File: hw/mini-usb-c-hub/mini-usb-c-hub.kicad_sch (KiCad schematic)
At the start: 26 parts, among them J1 USB_C_Receptacle_USB2.0_16P, U101 FE1.1s, Y101 12MHz

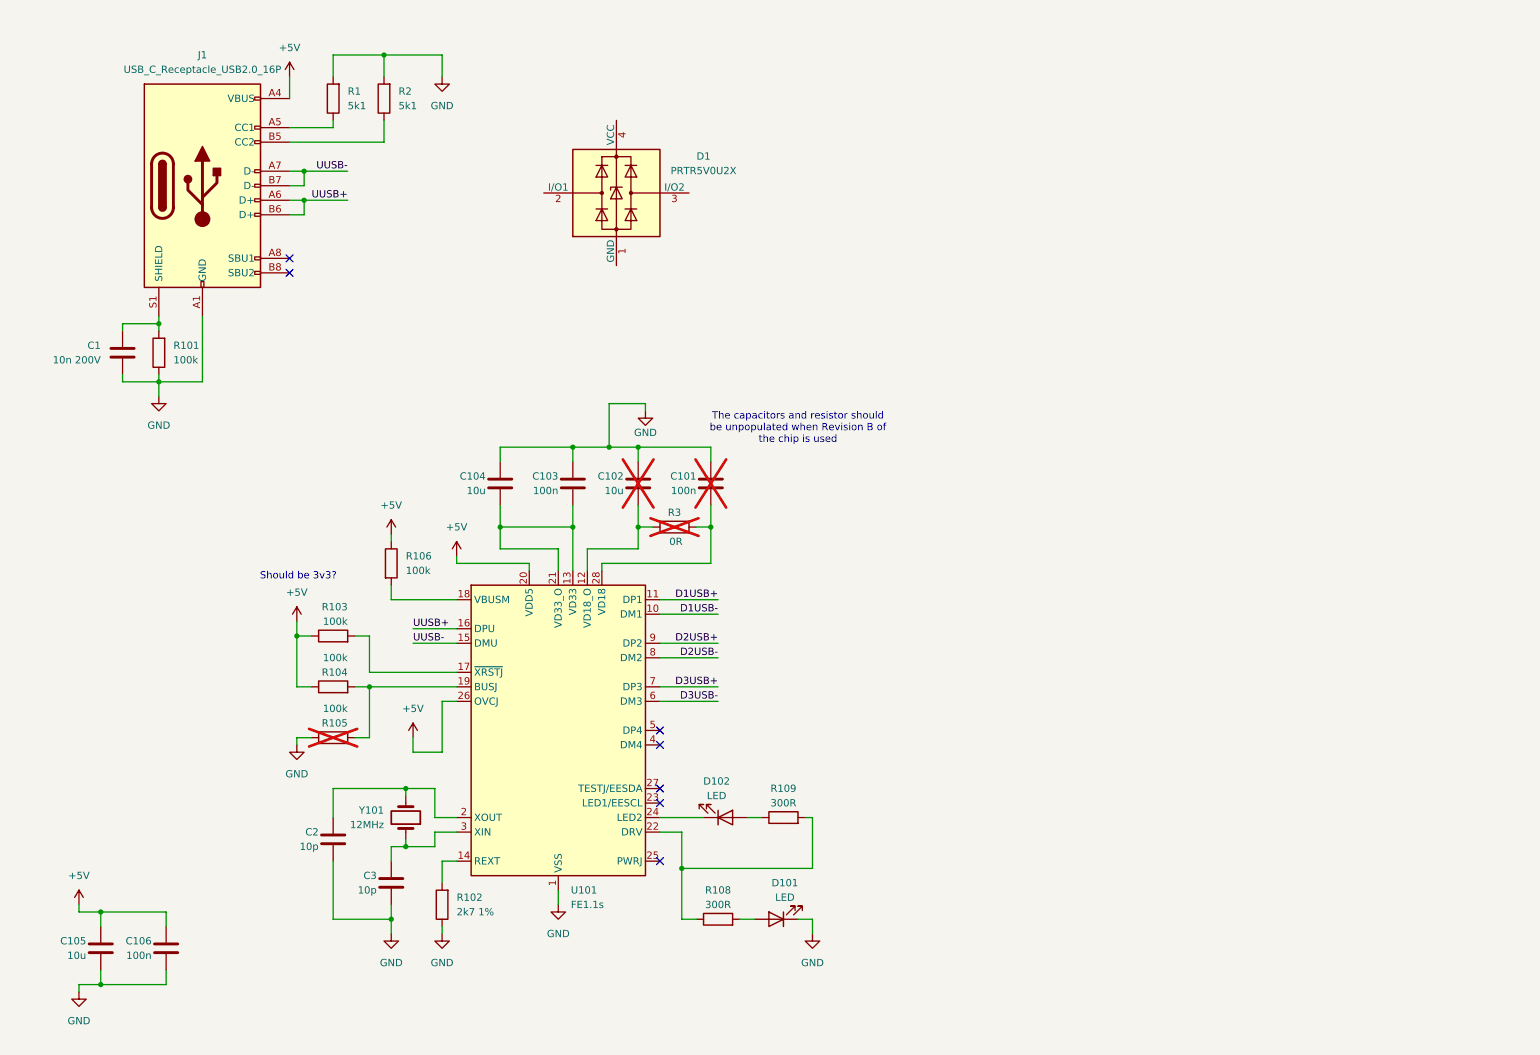
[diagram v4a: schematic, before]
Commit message: chore(hw): add downstream ports
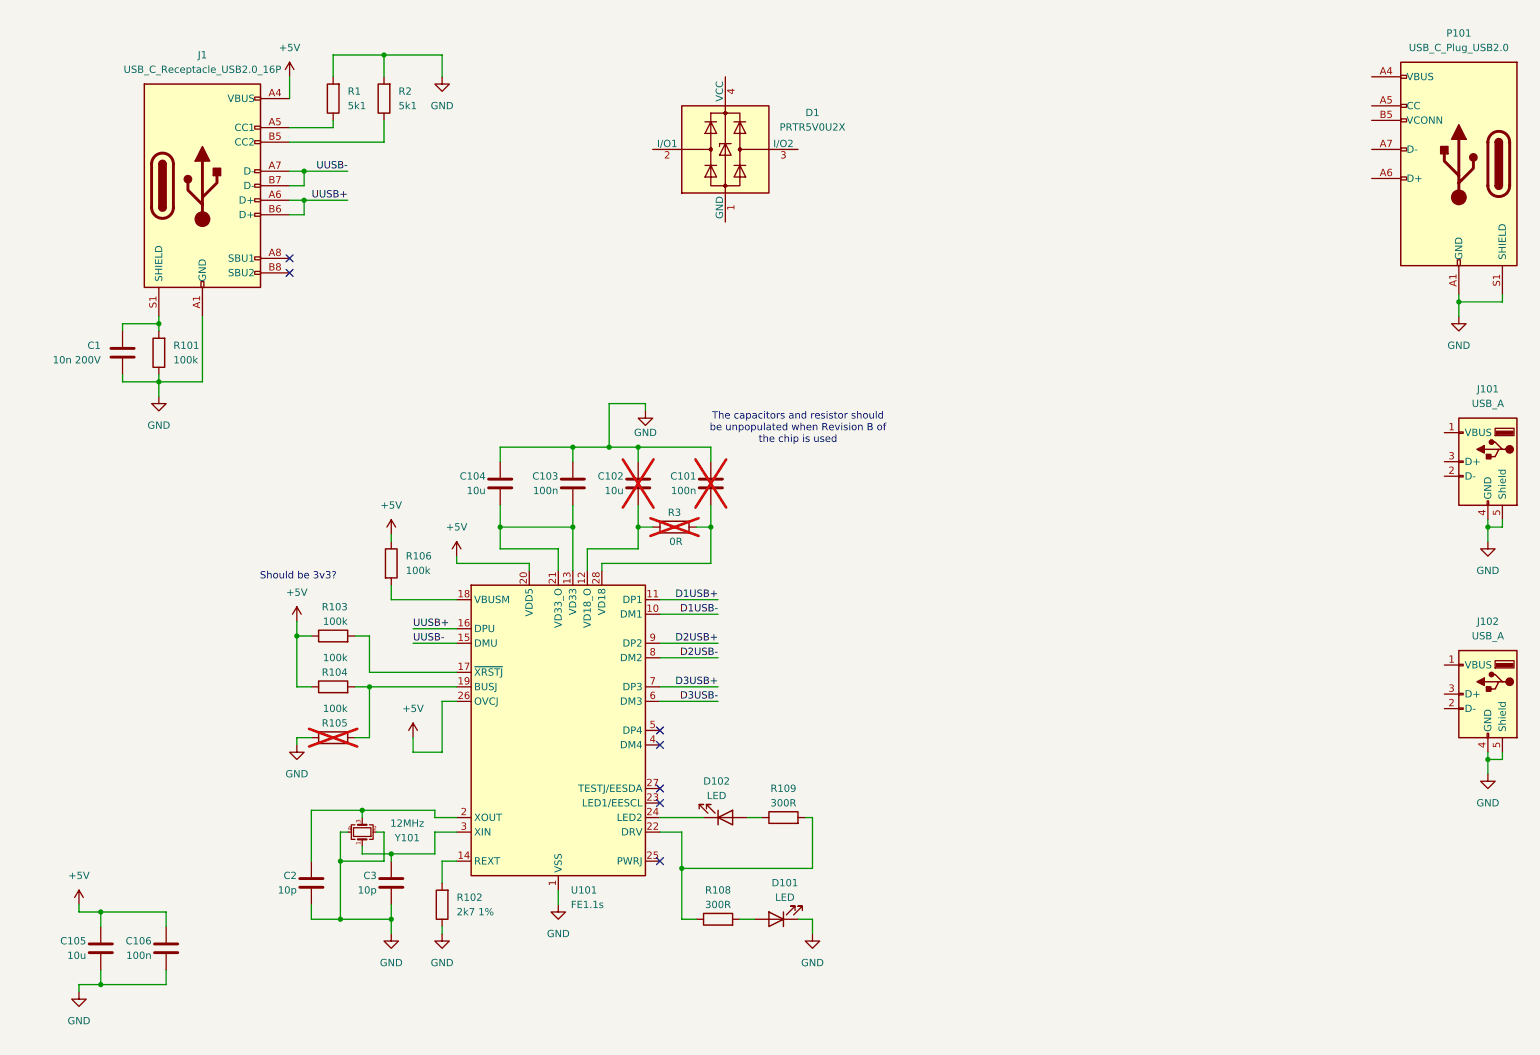
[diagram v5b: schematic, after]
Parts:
- removed Y101: 12MHz, symbol Device:Crystal
- added J101, J102: USB_A, Connector_USB:USB_A_Molex_67643_Horizontal, symbol Connector:USB_A
- added P101: USB_C_Plug_USB2.0, symbol Connector:USB_C_Plug_USB2.0
- added Y101: 12MHz, Crystal:Crystal_SMD_3225-4Pin_3.2x2.5mm_HandSoldering, symbol Device:Crystal_GND24_Small
- D101, D102: footprint (none) -> LED_SMD:LED_0805_2012Metric_Pad1.15x1.40mm_HandSolder
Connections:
- net GND: now also J101.4 (GND), J101.5 (Shield), J102.4 (GND), J102.5 (Shield), P101.A1 (GND), P101.A12 (GND), P101.B1 (GND), P101.B12 (GND), P101.S1 (SHIELD), Y101.2, Y101.4
- net at C2.2, U101.2 (XOUT): now also Y101.3
- net at C3.2, U101.3 (XIN): now also Y101.1
- new net: P101.A4 (VBUS), P101.A9 (VBUS), P101.B4 (VBUS), P101.B9 (VBUS)
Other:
- moved on the sheet: C2, D1

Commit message: chore(hw): add USB-C plug symbol
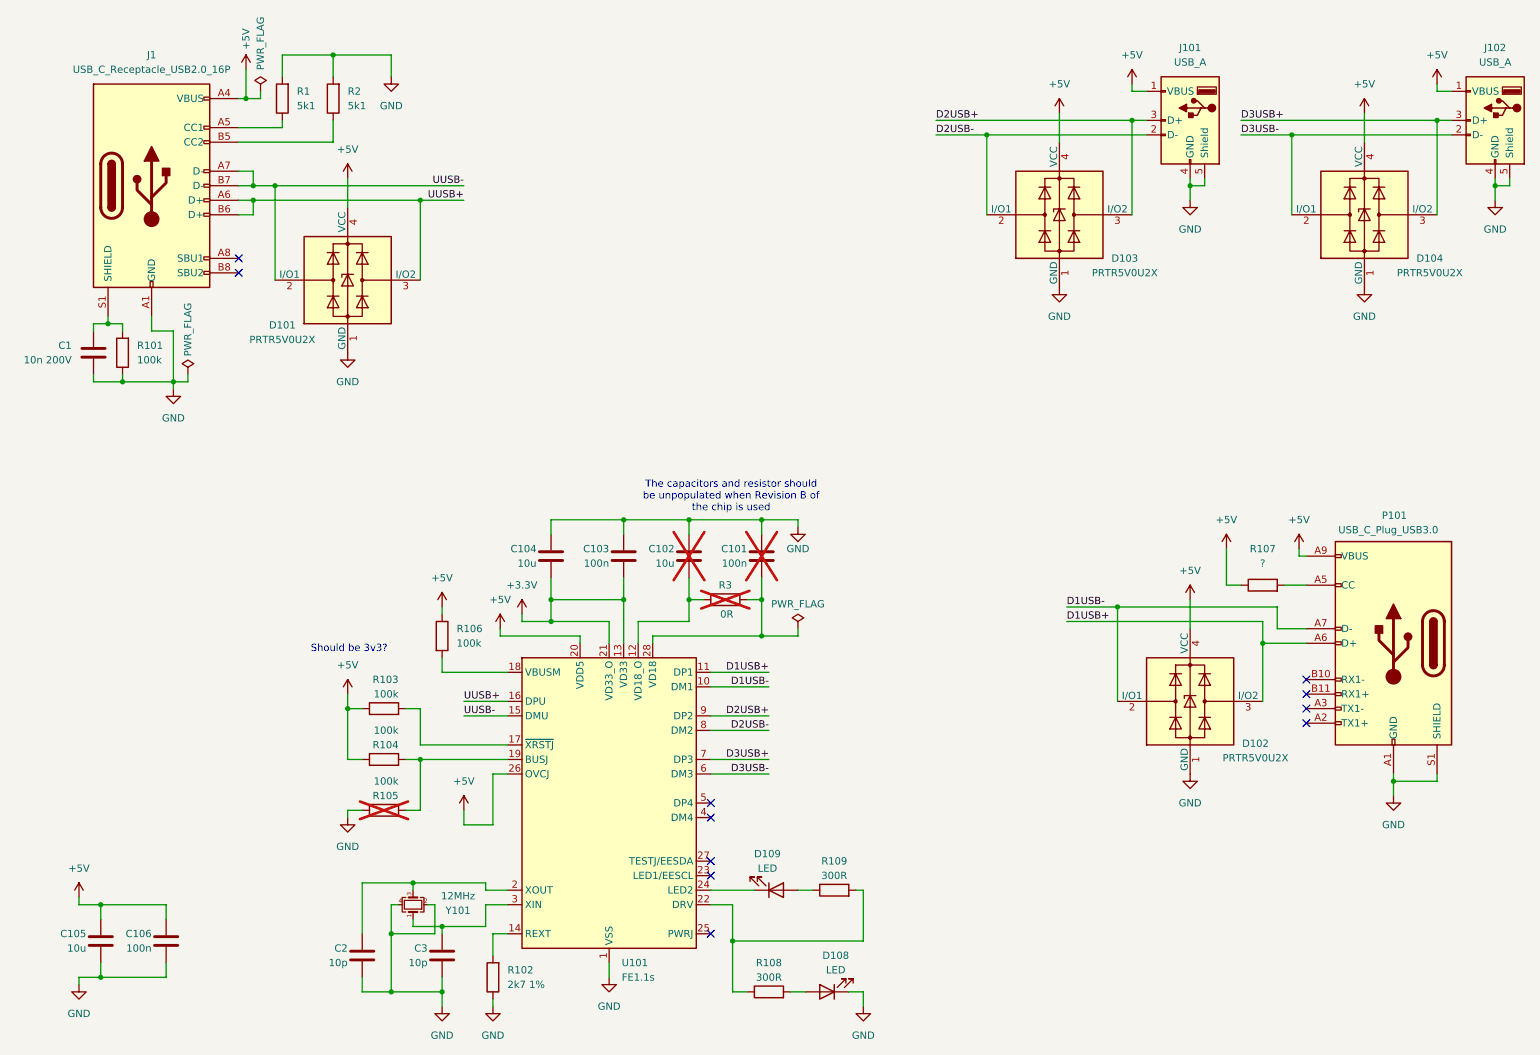
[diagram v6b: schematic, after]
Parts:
- removed P101: USB_C_Plug_USB2.0, symbol Connector:USB_C_Plug_USB2.0
- added D102, D103, D104: PRTR5V0U2X, Package_TO_SOT_SMD:SOT-143, symbol Power_Protection:PRTR5V0U2X
- added P101: USB_C_Plug_USB3.0, symbol local:USB_C_Plug_USB3.0
- added R107: ?, Resistor_SMD:R_0805_2012Metric_Pad1.20x1.40mm_HandSolder, symbol Device:R
- renumbered D1 to D101, D101 to D108, D102 to D109
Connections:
- net +5V: now also D101.4 (VCC), J101.1 (VBUS), J102.1 (VBUS), D102.4 (VCC), D103.4 (VCC), D104.4 (VCC), P101.A9 (VBUS), R107.1
- net D1USB+: now also D102.3 (I/O2), P101.A6 (D+)
- net D1USB-: now also D102.2 (I/O1), P101.A7 (D-)
- net D2USB+: now also J101.3 (D+), D103.3 (I/O2)
- net D2USB-: now also J101.2 (D-), D103.2 (I/O1)
- net D3USB+: now also J102.3 (D+), D104.3 (I/O2)
- net D3USB-: now also J102.2 (D-), D104.2 (I/O1)
- net GND: now also D101.1 (GND), D102.1 (GND), D103.1 (GND), D104.1 (GND), P101.A1 (GND), P101.S1 (SHIELD)
- net UUSB+: now also D101.3 (I/O2)
- net UUSB-: now also D101.2 (I/O1)
- net +3.3V: now reaches C103.1, C104.1, U101.13 (VD33), U101.21 (VD33_O)
- new net: P101.A5 (CC), R107.2
- no-connect marks 7 -> 11
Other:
- moved on the sheet: C1, C101, C102, C103, C104, C105, C106, C2, C3, D101, D108, D109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

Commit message: chore(hw): add USB-C plug footprint
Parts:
- P101: footprint (none) -> local:USB_C_Plug_G-Switch_GT-USB-8016A
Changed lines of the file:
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@@
 			)
 		)
-		(property "Footprint" ""
+		(property "Footprint" "local:USB_C_Plug_G-Switch_GT-USB-8016A"
 			(at 251.46 124.46 0)
 			(effects

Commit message: chore(hw): add some basic layout
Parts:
- removed D103, D104: PRTR5V0U2X, Package_TO_SOT_SMD:SOT-143, symbol Power_Protection:PRTR5V0U2X
- removed J101, J102: USB_A, Connector_USB:USB_A_Molex_67643_Horizontal, symbol Connector:USB_A
- renumbered J1 to J101
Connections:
- net D4USB-: now reaches U101.4 (DM4)
- net D4USB+: now reaches U101.5 (DP4)
- no-connect marks 11 -> 9
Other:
- added sheet Aux USB1 (aux-usb.kicad_sch)
- added sheet Aux USB2 (aux-usb.kicad_sch)
- added sheet Aux USB3 (aux-usb.kicad_sch)
- moved on the sheet: D102, P101, R107
